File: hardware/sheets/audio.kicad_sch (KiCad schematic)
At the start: 18 parts, among them J1 PicoGUS_LineIn, J2 LineOut_TRS, U1 MCP6002

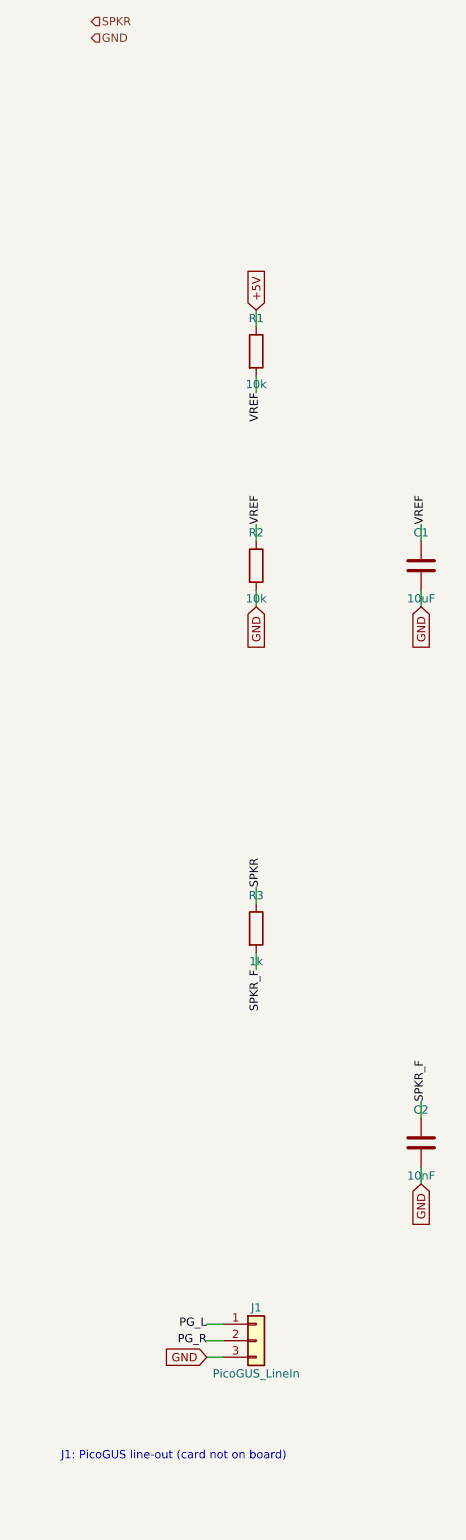
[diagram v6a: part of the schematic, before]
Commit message: PicoGUS on-board: chip-down transcription + shared RP2040 programming port
New picogus sheet (bank 13): a pin-faithful copy of polpo's PicoGUS 2.0
chip-down design (CERN-OHL-P, picogus/hw-chipdown sources) running STOCK
firmware -- the RP2040 GPIO map was extracted from the reference netlist
and our netlist matches it 30-for-30. Copied verbatim: the ADS-muxed
shared AD0-AD7 bus through SN74CB3T FET switches, the ~BUSOE power-up
latch (bus switches off until firmware first toggles ADS), AEN.DACK
IOR/IOW masking, open-drain IOCHRDY, APS6404L-3SQR sample PSRAM, PCM5102A
I2S DAC, IRQ/DMA jumper block (DMA must be jumpered to ch1, the only
MCU-serviced channel; IRQ5 is free since storage moved to IRQ14), AMS1117
local 3V3 island with ferrite-split AVDD/AGND, GPIO29-grounded board
detect, BOOTSEL + LED.

Deviations from the reference (user decisions, logged in
questions-picogus.md): no USB-A gameport (Supervisor owns HID; 0x201
unused), no wavetable header and no MIDI-out jack (build simplification --
the M62429 volume chip and passive mix node went with them; the firmware's
RV_CLK/RV_DATA/MIDI_TX pins are documented no-connects), no local audio
jack (RC-filtered DAC output leaves as PG_L/PG_R into the audio summer ->
the board's one line-out), no local programming USB.

Supervisor: crystal corrected to 30pF + 1k XOUT (same 12MHz part both
RP2040s -- fewer line items), BOOTSEL button added, and J6/SW2 form ONE
USB-C programming port for both bare RP2040s (DPDT slide: A = Supervisor,
C = PicoGUS; KiCad's SW_Slide_DPDT commons are the middle B pins -- the
first draft wired C as common and was corrected). J6 VBUS is unconnected:
the board must be powered to flash, so no back-power path exists.
PGUS_USB_DP/DM are a documented soft-card isolation exception (mxbus
PRIV_PROG); lifting the card means deleting them and fitting a connector.

Audio sheet: J1 line-in stub replaced by PG_L/PG_R interface pins.

Toolchain: six new flat symbols (CB3T3257/CB3T3245/74LVC2G06/PCM5102A/
M62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
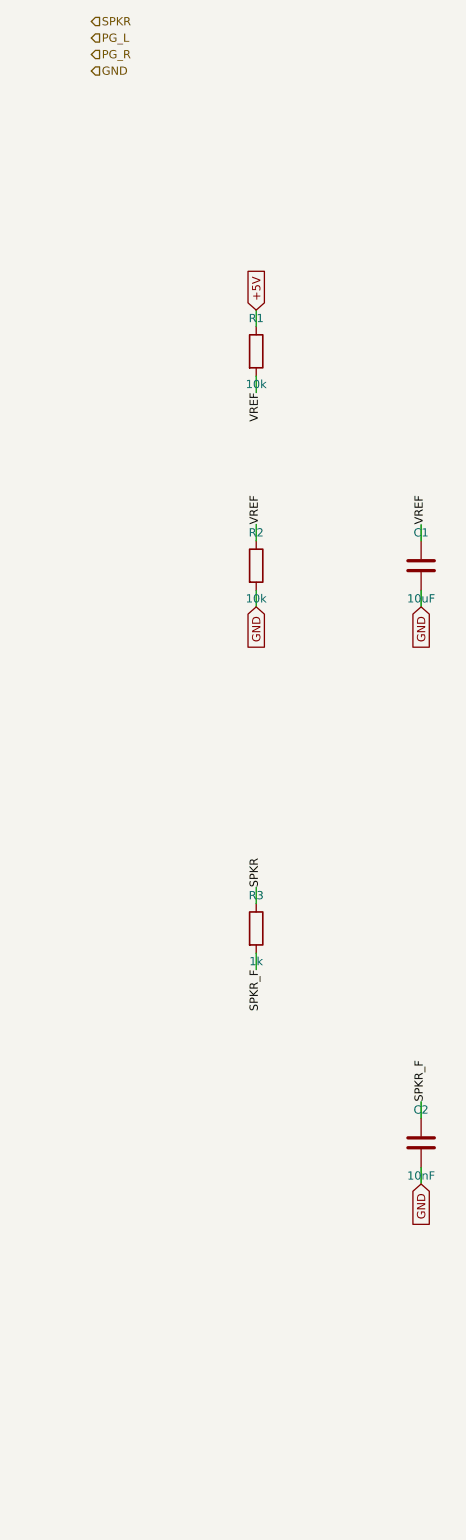
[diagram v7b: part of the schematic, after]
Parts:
- removed J1: PicoGUS_LineIn, symbol Connector_Generic:Conn_01x03
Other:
- note removed: "J1: PicoGUS line-out (card not on board)"
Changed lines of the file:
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@@
+		)
+	)
+	(hierarchical_label "PG_L"
+		(shape input)
+		(at 25.4 27.94 0)
+		(effects
+			(font
+				(size 1.27 1.27)
+			)
+		)
+	)
+	(hierarchical_label "PG_R"
+		(shape input)
+		(at 25.4 30.48 0)
+		(effects
+			(font
+				(size 1.27 1.27)
+			)
 		)
 	)
 	(hierarchical_label "GND"
 		(shape input)
-		(at 25.4 27.94 0)
+		(at 25.4 33.02 0)
 		(effects
 			(font
@@
 	(label "SPKR_AC"
 		(at 101.6 171.45 270)
-		(effects
-			(font
-				(size 1.27 1.27)
-			)
-		)
-	)
-	(wire
-		(pts
-			(xy 45.72 226.06)
-			(xy 43.18 226.06)
-		)
-		(stroke
-			(width 0)
-			(type default)
-		)
-	)
-	(label "PG_L"
-		(at 43.18 226.06 180)
-		(effects
-			(font
-				(size 1.27 1.27)
-			)
-		)
-	)
-	(wire
-		(pts
-			(xy 45.72 228.6)
-			(xy 43.18 228.6)
-		)
-		(stroke
-			(width 0)
-			(type default)
-		)
-	)
-	(label "PG_R"
-		(at 43.18 228.6 180)
-		(effects
-			(font
-				(size 1.27 1.27)
-			)
-		)
-	)
-	(wire
-		(pts
-			(xy 45.72 231.14)
-			(xy 43.18 231.14)
-		)
-		(stroke
-			(width 0)
-			(type default)
-		)
-	)
-	(global_label "GND"
-		(shape input)
-		(at 43.18 231.14 180)
-		(effects
-			(font
-				(size 1.27 1.27)
-			)
-		)
-	)
-	(text "J1: PicoGUS line-out (card not on board)"
-		(at 38.1 246.38 0)
 		(effects
 			(font
@@
 		(instances
 			(project "mini-xt"
-				(path "/26736c46-8b40-5460-874f-03596d17270c/de33a0b8-32a0-5c9f-9d2c-4a62e31bc235"
+				(path "/26736c46-8b40-5460-874f-03596d17270c/3608bfd0-7703-513a-bc2e-2c197268d7ed"
 					(reference "R1101")
 					(unit 1)
@@
 		(instances
 			(project "mini-xt"
-				(path "/26736c46-8b40-5460-874f-03596d17270c/de33a0b8-32a0-5c9f-9d2c-4a62e31bc235"
+				(path "/26736c46-8b40-5460-874f-03596d17270c/3608bfd0-7703-513a-bc2e-2c197268d7ed"
 					(reference "R1102")
 					(unit 1)
@@
 		(instances
 			(project "mini-xt"
-				(path "/26736c46-8b40-5460-874f-03596d17270c/de33a0b8-32a0-5c9f-9d2c-4a62e31bc235"
+				(path "/26736c46-8b40-5460-874f-03596d17270c/3608bfd0-7703-513a-bc2e-2c197268d7ed"
 					(reference "C1101")
 					(unit 1)
@@
 		(instances
 			(project "mini-xt"
-				(path "/26736c46-8b40-5460-874f-03596d17270c/de33a0b8-32a0-5c9f-9d2c-4a62e31bc235"
+				(path "/26736c46-8b40-5460-874f-03596d17270c/3608bfd0-7703-513a-bc2e-2c197268d7ed"
 					(reference "R1103")
 					(unit 1)
@@
 		(instances
 			(project "mini-xt"
-				(path "/26736c46-8b40-5460-874f-03596d17270c/de33a0b8-32a0-5c9f-9d2c-4a62e31bc235"
+				(path "/26736c46-8b40-5460-874f-03596d17270c/3608bfd0-7703-513a-bc2e-2c197268d7ed"
 					(reference "C1102")
 					(unit 1)
@@
 		(instances
 			(project "mini-xt"
-				(path "/26736c46-8b40-5460-874f-03596d17270c/de33a0b8-32a0-5c9f-9d2c-4a62e31bc235"
+				(path "/26736c46-8b40-5460-874f-03596d17270c/3608bfd0-7703-513a-bc2e-2c197268d7ed"
 					(reference "C1103")
-					(unit 1)
-				)
-			)
-		)
-	)
-	(symbol
-		(lib_id "Connector_Generic:Conn_01x03")
-		(at 50.8 228.6 0)
-		(unit 1)
-		(exclude_from_sim no)
-		(in_bom yes)
-		(on_board yes)
-		(dnp no)
-		(fields_autoplaced yes)
-		(property "Reference" "J1"
-			(at 50.8 223.52 0)
-			(effects
-				(font
-					(size 1.27 1.27)
-				)
-			)
-		)
-		(property "Value" "PicoGUS_LineIn"
-			(at 50.8 233.68 0)
-			(effects
-				(font
-					(size 1.27 1.27)
-				)
-			)
-		)
-		(property "Footprint" ""
-			(at 50.8 228.6 0)
-			(effects
-				(font
-					(size 1.27 1.27)
-				)
-				(hide yes)
-			)
-		)
-		(property "LCSC Part Num" "C2337"
-			(at 50.8 228.6 0)
-			(effects
-				(font
-					(size 1.27 1.27)
-				)
-				(hide yes)
-			)
-		)
-		(pin "1"
-		)
-		(pin "2"
-		)
-		(pin "3"
-		)
-		(instances
-			(project "mini-xt"
-				(path "/26736c46-8b40-5460-874f-03596d17270c/de33a0b8-32a0-5c9f-9d2c-4a62e31bc235"
-					(reference "J1101")
 					(unit 1)
 				)
@@
 		(instances
 			(project "mini-xt"
-				(path "/26736c46-8b40-5460-874f-03596d17270c/de33a0b8-32a0-5c9f-9d2c-4a62e31bc235"
+				(path "/26736c46-8b40-5460-874f-03596d17270c/3608bfd0-7703-513a-bc2e-2c197268d7ed"
 					(reference "C1104")
 					(unit 1)
@@
 		(instances
 			(project "mini-xt"
-				(path "/26736c46-8b40-5460-874f-03596d17270c/de33a0b8-32a0-5c9f-9d2c-4a62e31bc235"
+				(path "/26736c46-8b40-5460-874f-03596d17270c/3608bfd0-7703-513a-bc2e-2c197268d7ed"
 					(reference "C1105")
 					(unit 1)
@@
 		(instances
 			(project "mini-xt"
-				(path "/26736c46-8b40-5460-874f-03596d17270c/de33a0b8-32a0-5c9f-9d2c-4a62e31bc235"
+				(path "/26736c46-8b40-5460-874f-03596d17270c/3608bfd0-7703-513a-bc2e-2c197268d7ed"
 					(reference "U1101")
 					(unit 1)
@@
 		(instances
 			(project "mini-xt"
-				(path "/26736c46-8b40-5460-874f-03596d17270c/de33a0b8-32a0-5c9f-9d2c-4a62e31bc235"
+				(path "/26736c46-8b40-5460-874f-03596d17270c/3608bfd0-7703-513a-bc2e-2c197268d7ed"
 					(reference "C1106")
 					(unit 1)
@@
 		(instances
 			(project "mini-xt"
-				(path "/26736c46-8b40-5460-874f-03596d17270c/de33a0b8-32a0-5c9f-9d2c-4a62e31bc235"
+				(path "/26736c46-8b40-5460-874f-03596d17270c/3608bfd0-7703-513a-bc2e-2c197268d7ed"
 					(reference "R1104")
 					(unit 1)
@@
 		(instances
 			(project "mini-xt"
-				(path "/26736c46-8b40-5460-874f-03596d17270c/de33a0b8-32a0-5c9f-9d2c-4a62e31bc235"
+				(path "/26736c46-8b40-5460-874f-03596d17270c/3608bfd0-7703-513a-bc2e-2c197268d7ed"
 					(reference "R1105")
 					(unit 1)
@@
 		(instances
 			(project "mini-xt"
-				(path "/26736c46-8b40-5460-874f-03596d17270c/de33a0b8-32a0-5c9f-9d2c-4a62e31bc235"
+				(path "/26736c46-8b40-5460-874f-03596d17270c/3608bfd0-7703-513a-bc2e-2c197268d7ed"
 					(reference "R1110")
 					(unit 1)
@@
 		(instances
 			(project "mini-xt"
-				(path "/26736c46-8b40-5460-874f-03596d17270c/de33a0b8-32a0-5c9f-9d2c-4a62e31bc235"
+				(path "/26736c46-8b40-5460-874f-03596d17270c/3608bfd0-7703-513a-bc2e-2c197268d7ed"
 					(reference "R1106")
 					(unit 1)
@@
 		(instances
 			(project "mini-xt"
-				(path "/26736c46-8b40-5460-874f-03596d17270c/de33a0b8-32a0-5c9f-9d2c-4a62e31bc235"
+				(path "/26736c46-8b40-5460-874f-03596d17270c/3608bfd0-7703-513a-bc2e-2c197268d7ed"
 					(reference "R1107")
 					(unit 1)
@@
 		(instances
 			(project "mini-xt"
-				(path "/26736c46-8b40-5460-874f-03596d17270c/de33a0b8-32a0-5c9f-9d2c-4a62e31bc235"
+				(path "/26736c46-8b40-5460-874f-03596d17270c/3608bfd0-7703-513a-bc2e-2c197268d7ed"
 					(reference "C1107")
 					(unit 1)
@@
 		(instances
 			(project "mini-xt"
-				(path "/26736c46-8b40-5460-874f-03596d17270c/de33a0b8-32a0-5c9f-9d2c-4a62e31bc235"
+				(path "/26736c46-8b40-5460-874f-03596d17270c/3608bfd0-7703-513a-bc2e-2c197268d7ed"
 					(reference "J1102")
 					(unit 1)
